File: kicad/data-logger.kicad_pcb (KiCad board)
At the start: 2 copper layers, 37 x 46 mm, 34 parts, among them M1 M50-3130545, P1 PI4ULS3V501TAEX, P2 PI4ULS3V501TAEX, P3 PI4ULS3V501TAEX, P4 PI4ULS3V501TAEX, SW1 SW_Push, T1 TLV61225DCKR, Y1 32.768 kHz

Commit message: added reverse polarization protection
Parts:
- added U1: DMP2008UFG-7, data-logger:DMP2008UFG-7, F.Cu at (176.7, 114.8)
- moved C1 5.50 mm to (181.2, 112.0)
- moved L1 5.50 mm to (184.3, 114.8)
- moved T1 5.50 mm to (181.2, 114.8)
- moved C2 4.55 mm to (179.8, 117.5)
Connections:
- BT1 pad 1: /Power/2V4 -> Net-(BT1-Pad1)
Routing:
- net /Power/2V4: track 120.8 -> 138.2 mm, vias 3 -> 6
- net GND: track 32.8 -> 45.6 mm, vias 12 -> 11
- net Net-(BT1-Pad1): track 0.00 -> 9.62 mm
- net /Power/3V3: track 46.3 -> 38.1 mm
- net /SD Card/EN: track 48.6 -> 46.1 mm
- net Net-(L1-Pad1): track 4.11 -> 4.95 mm

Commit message: tweaks after drc
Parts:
- BT1: footprint Connector_PinSocket_2.54mm:PinSocket_1x02_P2.54mm_Horizontal -> data-logger:PinSocket_1x02_P2.54mm_Horizontal

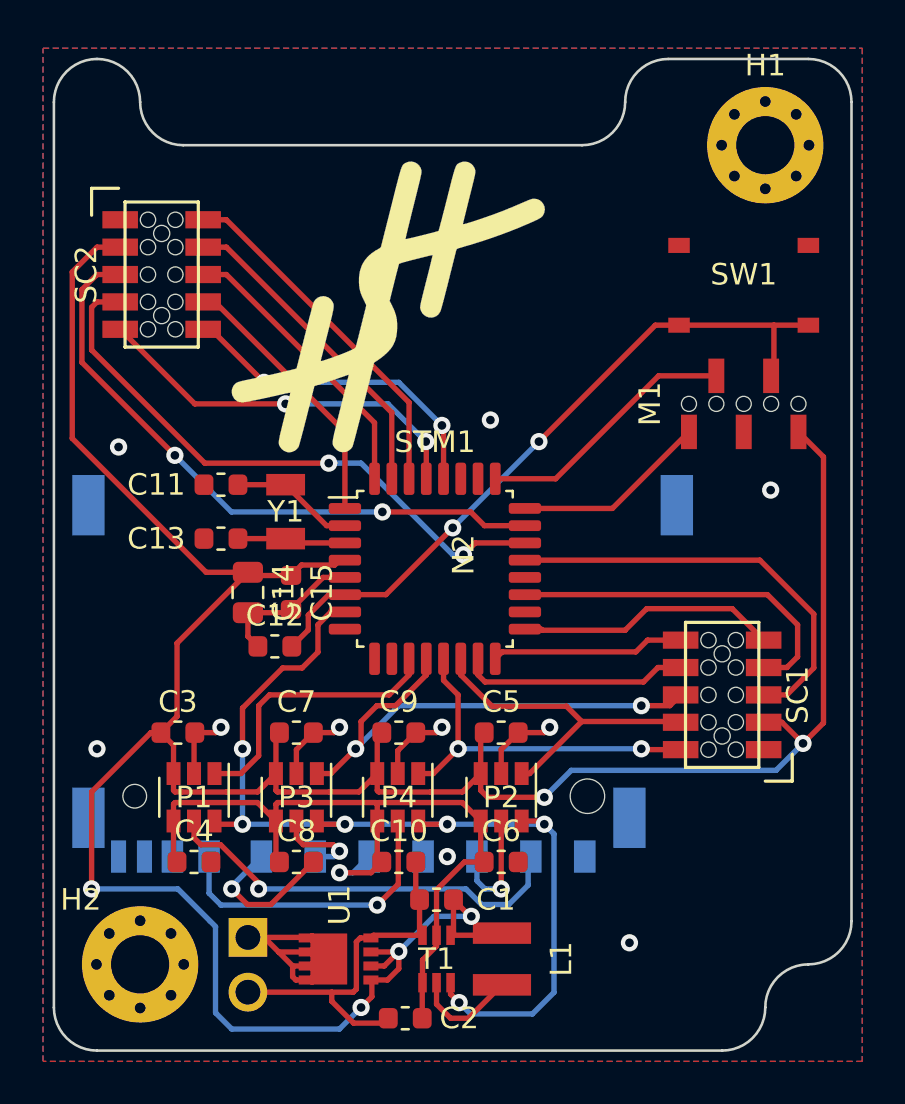
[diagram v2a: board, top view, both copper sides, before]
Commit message: updated sensor connector footprint
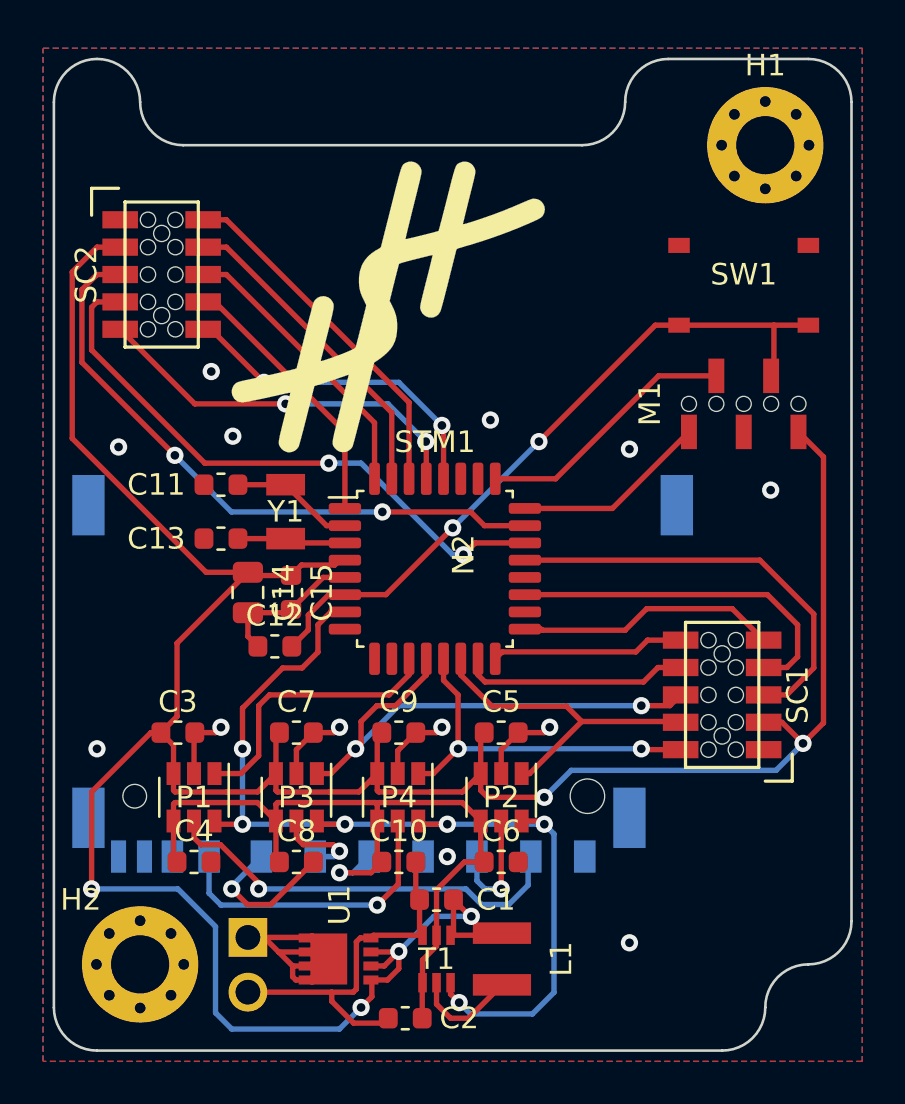
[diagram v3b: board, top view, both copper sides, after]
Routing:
- net GND: vias 11 -> 14

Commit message: added label
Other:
- board text added: "hochreiner.net data-logger V1.0.0"
